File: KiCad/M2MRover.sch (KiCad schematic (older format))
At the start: 27 parts, among them J1 Light Detection, J10 MPU6050 Gyro & Acc GY-521, J11 microbit_edge_connector, J12 ESP8266, J2 Serial (Bluetooth), J3 Servo, J4 H-Bridge, J5 Ultrasonic Down, J6 Ultrasonic Forward, J7 Compass GY-273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

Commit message: Replace ESP8266 connector with component
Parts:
- removed J12: ESP8266, Connector_PinSocket_2.54mm:PinSocket_2x04_P2.54mm_Vertical, symbol Connector_Generic:Conn_02x04_Odd_Even
- added U?: ESP8266-ESP-01, Connector_PinSocket_2.54mm:PinSocket_2x04_P2.54mm_Vertical, symbol MCU_Module_ESP8266:ESP8266-ESP-01
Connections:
- wire segments 188 -> 187
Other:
- moved on the sheet: R6, R7, R8, R9
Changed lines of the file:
@@
-$EndComp
-$Comp
-L Connector_Generic:Conn_02x04_Odd_Even J12
-U 1 1 5D647925
-P 5800 6050
-F 0 "J12" H 5850 6367 50  0000 C CNN
-F 1 "ESP8266" H 5850 6276 50  0000 C CNN
-F 2 "Connector_PinSocket_2.54mm:PinSocket_2x04_P2.54mm_Vertical" H 5800 6050 50  0001 C CNN
-F 3 "~" H 5800 6050 50  0001 C CNN
-	1    5800 6050
-	1    0    0    -1
 $EndComp
 $Comp
 L power:+3.3V #PWR010
 U 1 1 5D648646
-P 7150 5600
-F 0 "#PWR010" H 7150 5450 50  0001 C CNN
-F 1 "+3.3V" H 7165 5773 50  0000 C CNN
-F 2 "" H 7150 5600 50  0001 C CNN
-F 3 "" H 7150 5600 50  0001 C CNN
-	1    7150 5600
+P 5700 5400
+F 0 "#PWR010" H 5700 5250 50  0001 C CNN
+F 1 "+3.3V" H 5715 5573 50  0000 C CNN
+F 2 "" H 5700 5400 50  0001 C CNN
+F 3 "" H 5700 5400 50  0001 C CNN
+	1    5700 5400
 	1    0    0    -1
 $EndComp
@@
 L power:GND #PWR09
 U 1 1 5D6550DC
-P 5400 7050
-F 0 "#PWR09" H 5400 6800 50  0001 C CNN
-F 1 "GND" H 5405 6877 50  0000 C CNN
-F 2 "" H 5400 7050 50  0001 C CNN
-F 3 "" H 5400 7050 50  0001 C CNN
-	1    5400 7050
+P 5750 7200
+F 0 "#PWR09" H 5750 6950 50  0001 C CNN
+F 1 "GND" H 5755 7027 50  0000 C CNN
+F 2 "" H 5750 7200 50  0001 C CNN
+F 3 "" H 5750 7200 50  0001 C CNN
+	1    5750 7200
 	1    0    0    -1
 $EndComp
 Wire Wire Line
-	5600 5950 5400 5950
-Wire Wire Line
-	5400 5950 5400 6850
-Wire Wire Line
-	6100 6250 7150 6250
+	5350 6900 5350 7100
 $Comp
 L Device:R R9
 U 1 1 5D69B79B
-P 6850 5950
-F 0 "R9" H 6920 5996 50  0000 L CNN
-F 1 "10K" H 6920 5905 50  0000 L CNN
-F 2 "" V 6780 5950 50  0001 C CNN
-F 3 "~" H 6850 5950 50  0001 C CNN
-	1    6850 5950
+P 6350 6250
+F 0 "R9" H 6420 6296 50  0000 L CNN
+F 1 "10K" H 6420 6205 50  0000 L CNN
+F 2 "" V 6280 6250 50  0001 C CNN
+F 3 "~" H 6350 6250 50  0001 C CNN
+	1    6350 6250
 	1    0    0    -1
 $EndComp
@@
 L Device:R R8
 U 1 1 5D69BE85
-P 6550 5850
-F 0 "R8" H 6620 5896 50  0000 L CNN
-F 1 "10K" H 6620 5805 50  0000 L CNN
-F 2 "" V 6480 5850 50  0001 C CNN
-F 3 "~" H 6550 5850 50  0001 C CNN
-	1    6550 5850
+P 6100 5900
+F 0 "R8" H 6170 5946 50  0000 L CNN
+F 1 "10K" H 6170 5855 50  0000 L CNN
+F 2 "" V 6030 5900 50  0001 C CNN
+F 3 "~" H 6100 5900 50  0001 C CNN
+	1    6100 5900
 	1    0    0    -1
 $EndComp
 Wire Wire Line
-	6550 5700 6550 5650
+	6100 5750 6100 5600
 Wire Wire Line
-	6550 5650 7150 5650
-Connection ~ 7150 5650
+	6100 5600 6350 5600
 Wire Wire Line
-	7150 5650 7150 5600
+	6350 5600 6350 6100
 Wire Wire Line
-	7150 5650 7150 5800
-Wire Wire Line
-	6850 5800 7150 5800
-Connection ~ 7150 5800
-Wire Wire Line
-	7150 5800 7150 6250
-Wire Wire Line
-	6100 6050 6550 6050
-Wire Wire Line
-	6550 6050 6550 6000
-Wire Wire Line
-	6100 6150 6850 6150
-Wire Wire Line
-	6850 6150 6850 6100
+	5650 6400 6350 6400
 $Comp
 L Device:R R6
 U 1 1 5D776F56
-P 5100 5950
-F 0 "R6" H 5170 5996 50  0000 L CNN
-F 1 "1K" H 5170 5905 50  0000 L CNN
-F 2 "" V 5030 5950 50  0001 C CNN
-F 3 "~" H 5100 5950 50  0001 C CNN
-	1    5100 5950
+P 6700 6200
+F 0 "R6" H 6770 6246 50  0000 L CNN
+F 1 "1K" H 6770 6155 50  0000 L CNN
+F 2 "" V 6630 6200 50  0001 C CNN
+F 3 "~" H 6700 6200 50  0001 C CNN
+	1    6700 6200
 	1    0    0    -1
 $EndComp
@@
 L Device:R R7
 U 1 1 5D777435
-P 5100 6550
-F 0 "R7" H 5170 6596 50  0000 L CNN
-F 1 "2K" H 5170 6505 50  0000 L CNN
-F 2 "" V 5030 6550 50  0001 C CNN
-F 3 "~" H 5100 6550 50  0001 C CNN
-	1    5100 6550
+P 6700 6850
+F 0 "R7" H 6770 6896 50  0000 L CNN
+F 1 "2K" H 6770 6805 50  0000 L CNN
+F 2 "" V 6630 6850 50  0001 C CNN
+F 3 "~" H 6700 6850 50  0001 C CNN
+	1    6700 6850
 	1    0    0    -1
 $EndComp
-Text GLabel 5000 5700 0    50   Input ~ 0
+Text GLabel 6850 5800 2    50   Input ~ 0
 TX
 Wire Wire Line
-	5000 5700 5100 5700
+	6700 5800 6700 6050
 Wire Wire Line
-	5100 5700 5100 5800
+	6700 7000 6700 7100
 Wire Wire Line
-	5100 6700 5100 6850
+	6700 6350 6700 6500
 Wire Wire Line
-	5100 6850 5400 6850
-Connection ~ 5400 6850
+	5650 6500 6700 6500
+Connection ~ 6700 6500
 Wire Wire Line
-	5400 6850 5400 7050
-Wire Wire Line
-	5100 6100 5100 6250
-Wire Wire Line
-	5600 6250 5100 6250
-Connection ~ 5100 6250
-Wire Wire Line
-	5100 6250 5100 6400
-Text GLabel 6200 5950 2    50   Output ~ 0
+	6700 6500 6700 6700
+Text GLabel 5800 6000 2    50   Output ~ 0
 RX
 Wire Wire Line
-	6100 5950 6200 5950
-NoConn ~ 5600 6050
-NoConn ~ 5600 6150
+	5650 6000 5800 6000
+$Comp
+L MCU_Module_ESP8266:ESP8266-ESP-01 U?
+U 1 1 5D611E48
+P 5350 6250
+F 0 "U?" H 4873 6296 50  0000 R CNN
+F 1 "ESP8266-ESP-01" H 4873 6205 50  0000 R CNN
+F 2 "Connector_PinSocket_2.54mm:PinSocket_2x04_P2.54mm_Vertical" H 3950 5650 50  0001 C CNN
+F 3 "" H 4600 6750 50  0001 C CNN
+	1    5350 6250
+	1    0    0    -1
+$EndComp
+Wire Wire Line
+	5350 5600 5350 5400
+Wire Wire Line
+	5350 5400 5700 5400
+Wire Wire Line
+	5700 5400 6100 5400
+Wire Wire Line
+	6100 5400 6100 5600
+Connection ~ 5700 5400
+Connection ~ 6100 5600
+Wire Wire Line
+	6700 5800 6850 5800
+Wire Wire Line
+	6700 7100 5750 7100
+Wire Wire Line
+	5750 7200 5750 7100
+Connection ~ 5750 7100
+Wire Wire Line
+	5750 7100 5350 7100
+NoConn ~ 5650 6100
+NoConn ~ 5650 6300
+Wire Wire Line
+	5650 6200 6100 6200
+Wire Wire Line
+	6100 6200 6100 6050
 $EndSCHEMATC

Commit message: Add I2C pull up resistors
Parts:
- added R10, R11: 10K, symbol Device:R
- gave numbers to parts that had none: 1
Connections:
- net +5V: now also R10.1, R11.1
- net SCL: now also R11.2
- net SDA: now also R10.2
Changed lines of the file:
@@
 	5650 6000 5800 6000
 $Comp
-L MCU_Module_ESP8266:ESP8266-ESP-01 U?
+L MCU_Module_ESP8266:ESP8266-ESP-01 U2
 U 1 1 5D611E48
 P 5350 6250
-F 0 "U?" H 4873 6296 50  0000 R CNN
+F 0 "U2" H 4873 6296 50  0000 R CNN
 F 1 "ESP8266-ESP-01" H 4873 6205 50  0000 R CNN
 F 2 "Connector_PinSocket_2.54mm:PinSocket_2x04_P2.54mm_Vertical" H 3950 5650 50  0001 C CNN
@@
 Wire Wire Line
 	6100 6200 6100 6050
+Text GLabel 7700 5550 0    50   BiDi ~ 0
+SDA
+Text GLabel 7700 5650 0    50   BiDi ~ 0
+SCL
+$Comp
+L Device:R R10
+U 1 1 5D68795D
+P 7950 5250
+F 0 "R10" H 8020 5296 50  0000 L CNN
+F 1 "10K" H 8020 5205 50  0000 L CNN
+F 2 "" V 7880 5250 50  0001 C CNN
+F 3 "~" H 7950 5250 50  0001 C CNN
+	1    7950 5250
+	1    0    0    -1
+$EndComp
+$Comp
+L Device:R R11
+U 1 1 5D6882C9
+P 8350 5250
+F 0 "R11" H 8420 5296 50  0000 L CNN
+F 1 "10K" H 8420 5205 50  0000 L CNN
+F 2 "" V 8280 5250 50  0001 C CNN
+F 3 "~" H 8350 5250 50  0001 C CNN
+	1    8350 5250
+	1    0    0    -1
+$EndComp
+$Comp
+L power:+5V #PWR0116
+U 1 1 5D688A7F
+P 8150 4850
+F 0 "#PWR0116" H 8150 4700 50  0001 C CNN
+F 1 "+5V" H 8165 5023 50  0000 C CNN
+F 2 "" H 8150 4850 50  0001 C CNN
+F 3 "" H 8150 4850 50  0001 C CNN
+	1    8150 4850
+	1    0    0    -1
+$EndComp
+Wire Wire Line
+	7700 5550 7950 5550
+Wire Wire Line
+	7950 5550 7950 5400
+Wire Wire Line
+	7700 5650 8350 5650
+Wire Wire Line
+	8350 5650 8350 5400
+Wire Wire Line
+	7950 5100 7950 4950
+Wire Wire Line
+	7950 4950 8150 4950
+Wire Wire Line
+	8350 4950 8350 5100
+Wire Wire Line
+	8150 4850 8150 4950
+Connection ~ 8150 4950
+Wire Wire Line
+	8150 4950 8350 4950
 $EndSCHEMATC

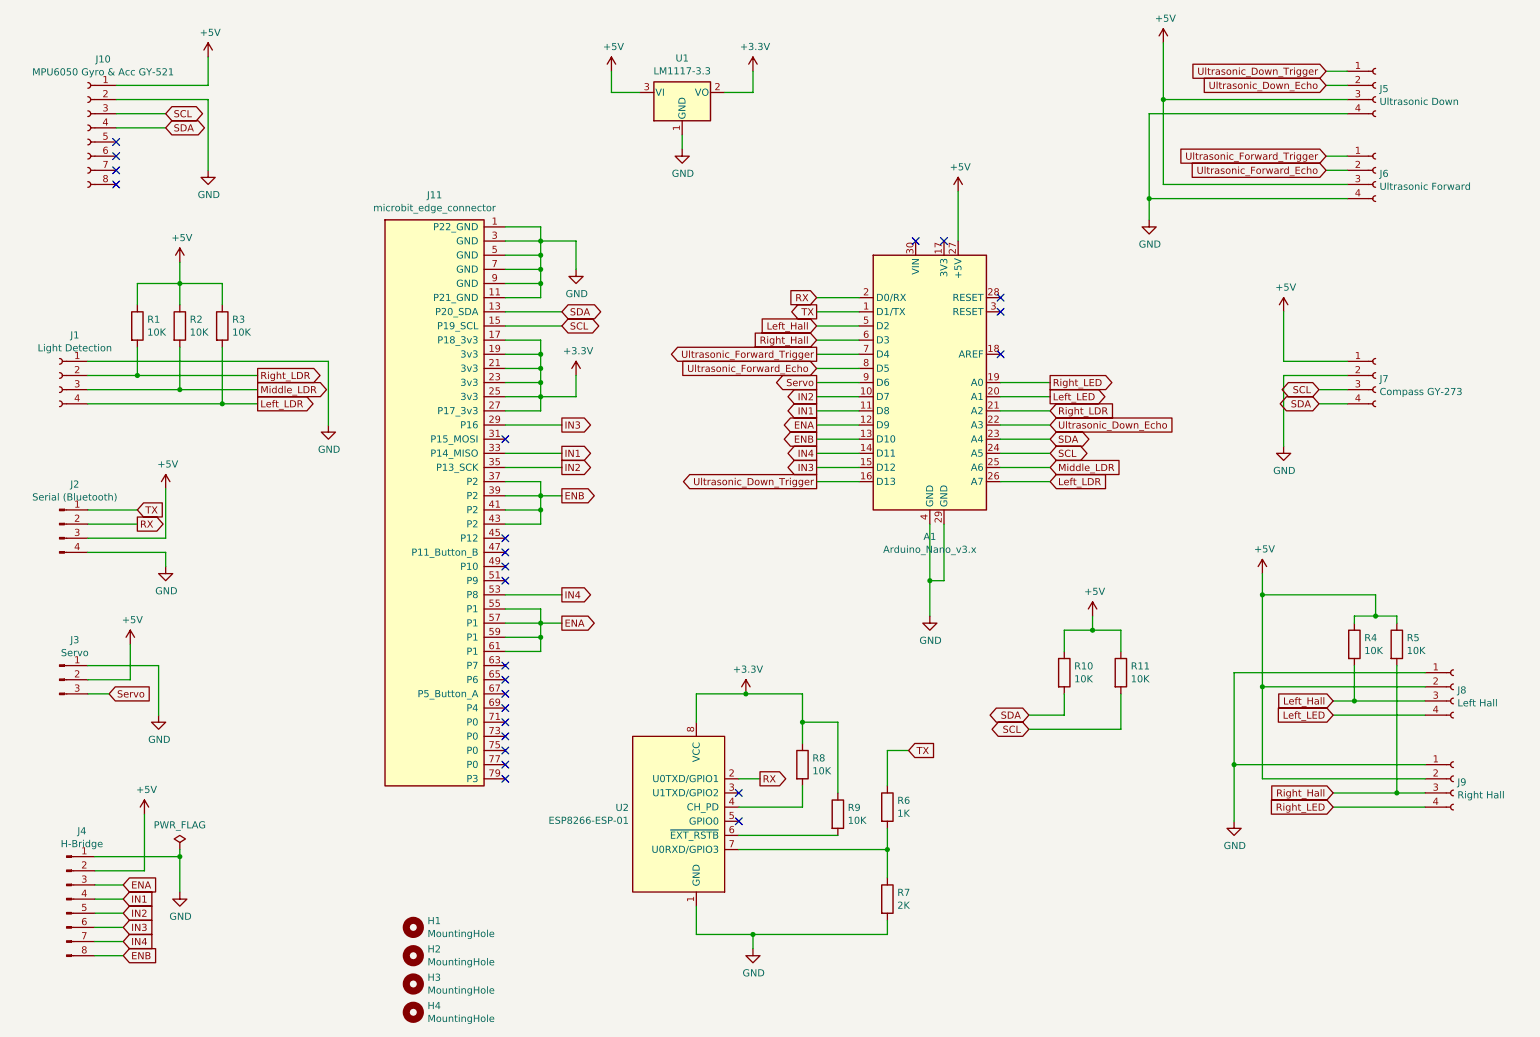
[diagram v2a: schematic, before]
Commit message: Add capacitors to PWM output for EMC
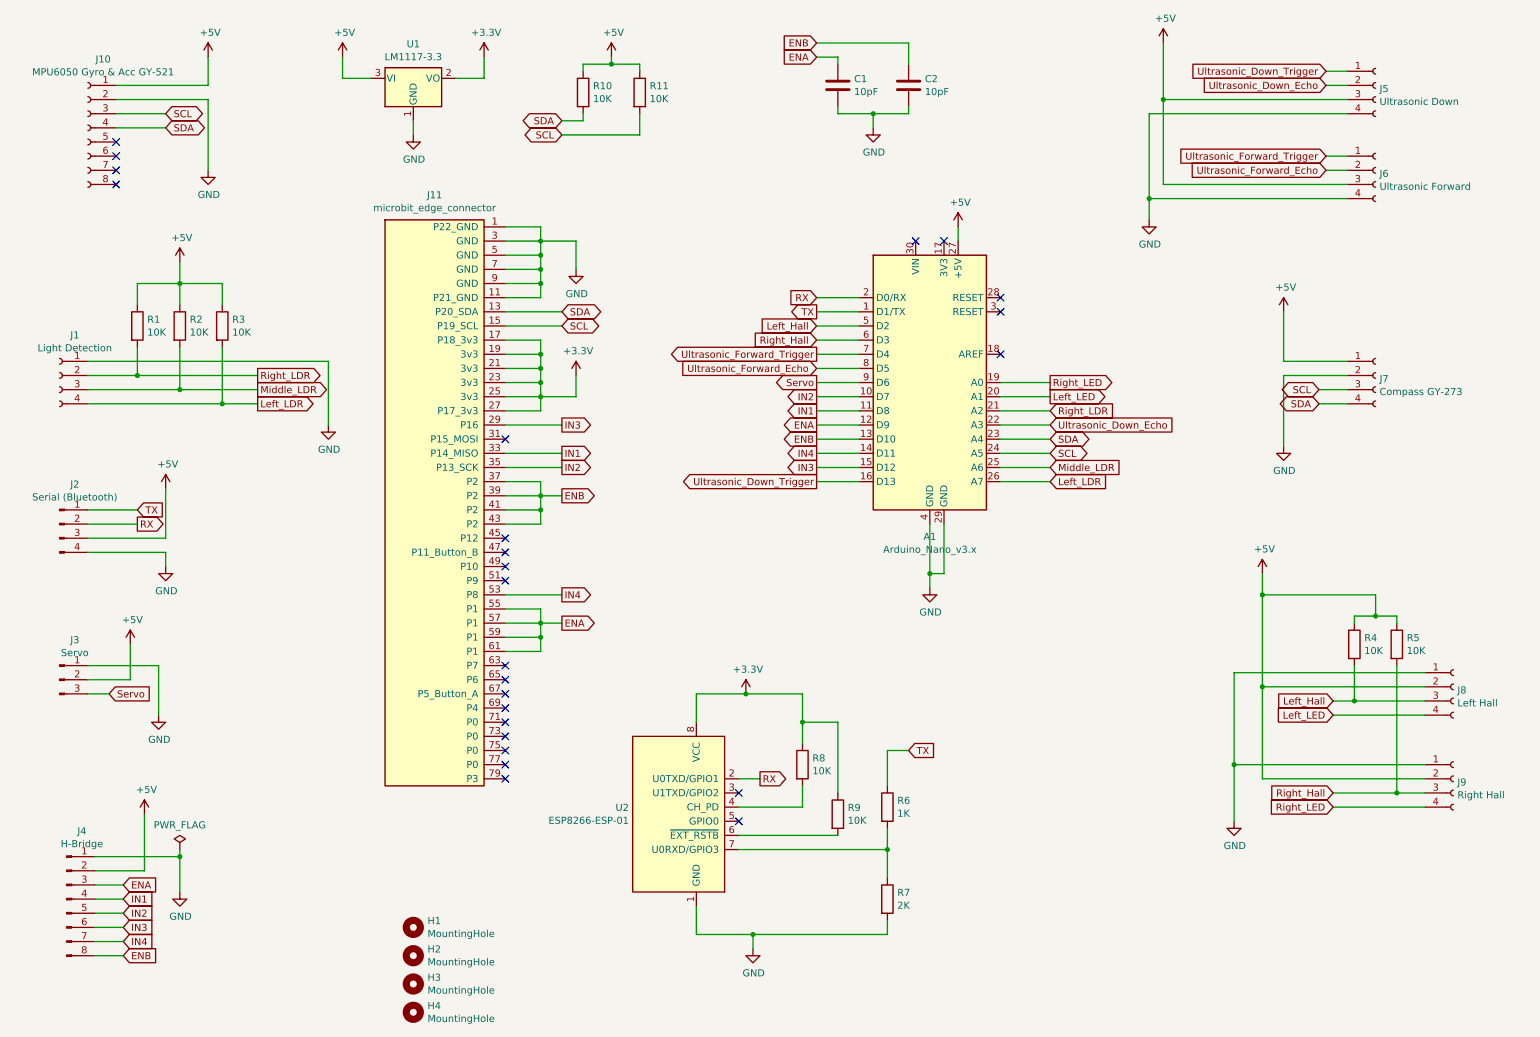
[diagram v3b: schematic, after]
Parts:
- added C1, C2: 10pF, symbol Device:C
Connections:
- net ENA: now also C1.1
- net ENB: now also C2.1
- net GND: now also C1.2, C2.2
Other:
- moved on the sheet: R10, R11, U1
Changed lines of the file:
@@
 L power:GND #PWR0101
 U 1 1 5D59C0F1
-P 7000 4850
-F 0 "#PWR0101" H 7000 4600 50  0001 C CNN
-F 1 "GND" H 7005 4677 50  0000 C CNN
-F 2 "" H 7000 4850 50  0001 C CNN
-F 3 "" H 7000 4850 50  0001 C CNN
-	1    7000 4850
-	1    0    0    -1
-$EndComp
-Wire Wire Line
-	7000 4200 7000 4600
-Wire Wire Line
-	7100 4200 7100 4600
-Wire Wire Line
-	7100 4600 7000 4600
-Connection ~ 7000 4600
-Wire Wire Line
-	7000 4600 7000 4850
+P 7000 4650
+F 0 "#PWR0101" H 7000 4400 50  0001 C CNN
+F 1 "GND" H 7005 4477 50  0000 C CNN
+F 2 "" H 7000 4650 50  0001 C CNN
+F 3 "" H 7000 4650 50  0001 C CNN
+	1    7000 4650
+	1    0    0    -1
+$EndComp
+Wire Wire Line
+	7000 4200 7000 4550
+Wire Wire Line
+	7100 4200 7100 4550
+Wire Wire Line
+	7100 4550 7000 4550
+Connection ~ 7000 4550
+Wire Wire Line
+	7000 4550 7000 4650
 $Comp
 L power:+5V #PWR0102
 U 1 1 5D59D72C
-P 7200 1850
-F 0 "#PWR0102" H 7200 1700 50  0001 C CNN
-F 1 "+5V" H 7215 2023 50  0000 C CNN
-F 2 "" H 7200 1850 50  0001 C CNN
-F 3 "" H 7200 1850 50  0001 C CNN
-	1    7200 1850
-	1    0    0    -1
-$EndComp
-Wire Wire Line
-	7200 1850 7200 2200
+P 7200 2100
+F 0 "#PWR0102" H 7200 1950 50  0001 C CNN
+F 1 "+5V" H 7215 2273 50  0000 C CNN
+F 2 "" H 7200 2100 50  0001 C CNN
+F 3 "" H 7200 2100 50  0001 C CNN
+	1    7200 2100
+	1    0    0    -1
+$EndComp
+Wire Wire Line
+	7200 2100 7200 2200
 $Comp
 L power:GND #PWR0103
@@
 L Regulator_Linear:LM1117-3.3 U1
 U 1 1 5D5D0567
-P 5250 1150
-F 0 "U1" H 5250 1392 50  0000 C CNN
-F 1 "LM1117-3.3" H 5250 1301 50  0000 C CNN
-F 2 "Package_TO_SOT_THT:TO-220-3_Vertical" H 5250 1150 50  0001 C CNN
-F 3 "http://www.ti.com/lit/ds/symlink/lm1117.pdf" H 5250 1150 50  0001 C CNN
-	1    5250 1150
+P 3350 1050
+F 0 "U1" H 3350 1292 50  0000 C CNN
+F 1 "LM1117-3.3" H 3350 1201 50  0000 C CNN
+F 2 "Package_TO_SOT_THT:TO-220-3_Vertical" H 3350 1050 50  0001 C CNN
+F 3 "http://www.ti.com/lit/ds/symlink/lm1117.pdf" H 3350 1050 50  0001 C CNN
+	1    3350 1050
 	1    0    0    -1
 $EndComp
@@
 L power:+5V #PWR06
 U 1 1 5D5DDFD0
-P 4750 1000
-F 0 "#PWR06" H 4750 850 50  0001 C CNN
-F 1 "+5V" H 4765 1173 50  0000 C CNN
-F 2 "" H 4750 1000 50  0001 C CNN
-F 3 "" H 4750 1000 50  0001 C CNN
-	1    4750 1000
+P 2850 900
+F 0 "#PWR06" H 2850 750 50  0001 C CNN
+F 1 "+5V" H 2865 1073 50  0000 C CNN
+F 2 "" H 2850 900 50  0001 C CNN
+F 3 "" H 2850 900 50  0001 C CNN
+	1    2850 900
 	1    0    0    -1
 $EndComp
@@
 L power:+3.3V #PWR08
 U 1 1 5D5DE8F7
-P 5750 1000
-F 0 "#PWR08" H 5750 850 50  0001 C CNN
-F 1 "+3.3V" H 5765 1173 50  0000 C CNN
-F 2 "" H 5750 1000 50  0001 C CNN
-F 3 "" H 5750 1000 50  0001 C CNN
-	1    5750 1000
+P 3850 900
+F 0 "#PWR08" H 3850 750 50  0001 C CNN
+F 1 "+3.3V" H 3865 1073 50  0000 C CNN
+F 2 "" H 3850 900 50  0001 C CNN
+F 3 "" H 3850 900 50  0001 C CNN
+	1    3850 900
 	1    0    0    -1
 $EndComp
@@
 L power:GND #PWR07
 U 1 1 5D5DF372
-P 5250 1550
-F 0 "#PWR07" H 5250 1300 50  0001 C CNN
-F 1 "GND" H 5255 1377 50  0000 C CNN
-F 2 "" H 5250 1550 50  0001 C CNN
-F 3 "" H 5250 1550 50  0001 C CNN
-	1    5250 1550
-	1    0    0    -1
-$EndComp
-Wire Wire Line
-	4750 1000 4750 1150
-Wire Wire Line
-	4750 1150 4950 1150
-Wire Wire Line
-	5550 1150 5750 1150
-Wire Wire Line
-	5750 1150 5750 1000
-Wire Wire Line
-	5250 1450 5250 1550
+P 3350 1450
+F 0 "#PWR07" H 3350 1200 50  0001 C CNN
+F 1 "GND" H 3355 1277 50  0000 C CNN
+F 2 "" H 3350 1450 50  0001 C CNN
+F 3 "" H 3350 1450 50  0001 C CNN
+	1    3350 1450
+	1    0    0    -1
+$EndComp
+Wire Wire Line
+	2850 900  2850 1050
+Wire Wire Line
+	2850 1050 3050 1050
+Wire Wire Line
+	3650 1050 3850 1050
+Wire Wire Line
+	3850 1050 3850 900
+Wire Wire Line
+	3350 1350 3350 1450
 Wire Wire Line
 	4000 3500 4400 3500
@@
 Wire Wire Line
 	6100 6200 6100 6050
-Text GLabel 7700 5550 0    50   BiDi ~ 0
+Text GLabel 4400 1350 0    50   BiDi ~ 0
 SDA
-Text GLabel 7700 5650 0    50   BiDi ~ 0
+Text GLabel 4400 1450 0    50   BiDi ~ 0
 SCL
 $Comp
 L Device:R R10
 U 1 1 5D68795D
-P 7950 5250
-F 0 "R10" H 8020 5296 50  0000 L CNN
-F 1 "10K" H 8020 5205 50  0000 L CNN
-F 2 "" V 7880 5250 50  0001 C CNN
-F 3 "~" H 7950 5250 50  0001 C CNN
-	1    7950 5250
+P 4550 1150
+F 0 "R10" H 4620 1196 50  0000 L CNN
+F 1 "10K" H 4620 1105 50  0000 L CNN
+F 2 "" V 4480 1150 50  0001 C CNN
+F 3 "~" H 4550 1150 50  0001 C CNN
+	1    4550 1150
 	1    0    0    -1
 $EndComp
@@
 L Device:R R11
 U 1 1 5D6882C9
-P 8350 5250
-F 0 "R11" H 8420 5296 50  0000 L CNN
-F 1 "10K" H 8420 5205 50  0000 L CNN
-F 2 "" V 8280 5250 50  0001 C CNN
-F 3 "~" H 8350 5250 50  0001 C CNN
-	1    8350 5250
+P 4950 1150
+F 0 "R11" H 5020 1196 50  0000 L CNN
+F 1 "10K" H 5020 1105 50  0000 L CNN
+F 2 "" V 4880 1150 50  0001 C CNN
+F 3 "~" H 4950 1150 50  0001 C CNN
+	1    4950 1150
 	1    0    0    -1
 $EndComp
@@
 L power:+5V #PWR0116
 U 1 1 5D688A7F
-P 8150 4850
-F 0 "#PWR0116" H 8150 4700 50  0001 C CNN
-F 1 "+5V" H 8165 5023 50  0000 C CNN
-F 2 "" H 8150 4850 50  0001 C CNN
-F 3 "" H 8150 4850 50  0001 C CNN
-	1    8150 4850
-	1    0    0    -1
-$EndComp
-Wire Wire Line
-	7700 5550 7950 5550
-Wire Wire Line
-	7950 5550 7950 5400
-Wire Wire Line
-	7700 5650 8350 5650
-Wire Wire Line
-	8350 5650 8350 5400
-Wire Wire Line
-	7950 5100 7950 4950
-Wire Wire Line
-	7950 4950 8150 4950
-Wire Wire Line
-	8350 4950 8350 5100
-Wire Wire Line
-	8150 4850 8150 4950
-Connection ~ 8150 4950
-Wire Wire Line
-	8150 4950 8350 4950
+P 4750 900
+F 0 "#PWR0116" H 4750 750 50  0001 C CNN
+F 1 "+5V" H 4765 1073 50  0000 C CNN
+F 2 "" H 4750 900 50  0001 C CNN
+F 3 "" H 4750 900 50  0001 C CNN
+	1    4750 900
+	1    0    0    -1
+$EndComp
+Wire Wire Line
+	4400 1350 4550 1350
+Wire Wire Line
+	4550 1350 4550 1300
+Wire Wire Line
+	4400 1450 4950 1450
+Wire Wire Line
+	4950 1450 4950 1300
+Wire Wire Line
+	4550 1000 4550 950
+Wire Wire Line
+	4550 950  4750 950
+Wire Wire Line
+	4950 950  4950 1000
+Wire Wire Line
+	4750 900  4750 950
+Connection ~ 4750 950
+Wire Wire Line
+	4750 950  4950 950
+$Comp
+L power:GND #PWR0117
+U 1 1 5D81F247
+P 6600 1400
+F 0 "#PWR0117" H 6600 1150 50  0001 C CNN
+F 1 "GND" H 6605 1227 50  0000 C CNN
+F 2 "" H 6600 1400 50  0001 C CNN
+F 3 "" H 6600 1400 50  0001 C CNN
+	1    6600 1400
+	1    0    0    -1
+$EndComp
+$Comp
+L Device:C C1
+U 1 1 5D832319
+P 6350 1100
+F 0 "C1" H 6465 1146 50  0000 L CNN
+F 1 "10pF" H 6465 1055 50  0000 L CNN
+F 2 "" H 6388 950 50  0001 C CNN
+F 3 "~" H 6350 1100 50  0001 C CNN
+	1    6350 1100
+	1    0    0    -1
+$EndComp
+$Comp
+L Device:C C2
+U 1 1 5D832B5B
+P 6850 1100
+F 0 "C2" H 6965 1146 50  0000 L CNN
+F 1 "10pF" H 6965 1055 50  0000 L CNN
+F 2 "" H 6888 950 50  0001 C CNN
+F 3 "~" H 6850 1100 50  0001 C CNN
+	1    6850 1100
+	1    0    0    -1
+$EndComp
+Text GLabel 6200 900  0    50   Input ~ 0
+ENA
+Text GLabel 6200 800  0    50   Input ~ 0
+ENB
+Wire Wire Line
+	6350 1250 6350 1300
+Wire Wire Line
+	6350 1300 6600 1300
+Wire Wire Line
+	6850 1300 6850 1250
+Wire Wire Line
+	6600 1400 6600 1300
+Connection ~ 6600 1300
+Wire Wire Line
+	6600 1300 6850 1300
+Wire Wire Line
+	6200 900  6350 900
+Wire Wire Line
+	6350 900  6350 950
+Wire Wire Line
+	6200 800  6850 800
+Wire Wire Line
+	6850 800  6850 950
 $EndSCHEMATC
